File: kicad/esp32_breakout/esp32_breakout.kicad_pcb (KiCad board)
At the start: 2 copper layers, 70 x 35 mm, 26 parts, among them J1 JST B5B-PH-K-S, J10 JST B6B-PH-K-S, J2 JST B5B-PH-K-S, J3 JST B7B-PH-K-S, J4 XT30U-M, J5 HDR F 2.54MM VERT, J6 HDR F 2.54MM 5-pin VERT, J9 JST B6B-PH-K-S, SW1 SS12D10, U1 ESP32 DEV KIT Module 30-pin, U2 LM2596 Module

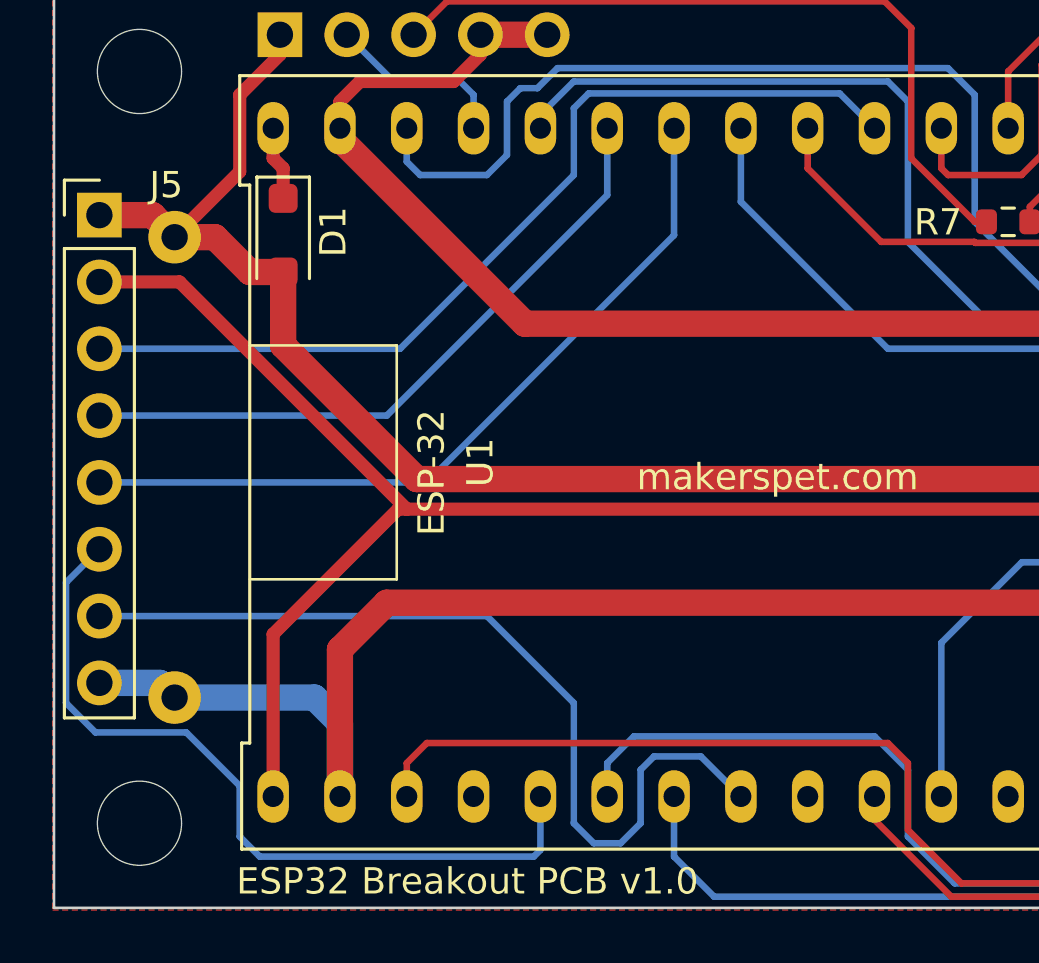
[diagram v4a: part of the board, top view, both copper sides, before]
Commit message: Footprint fix
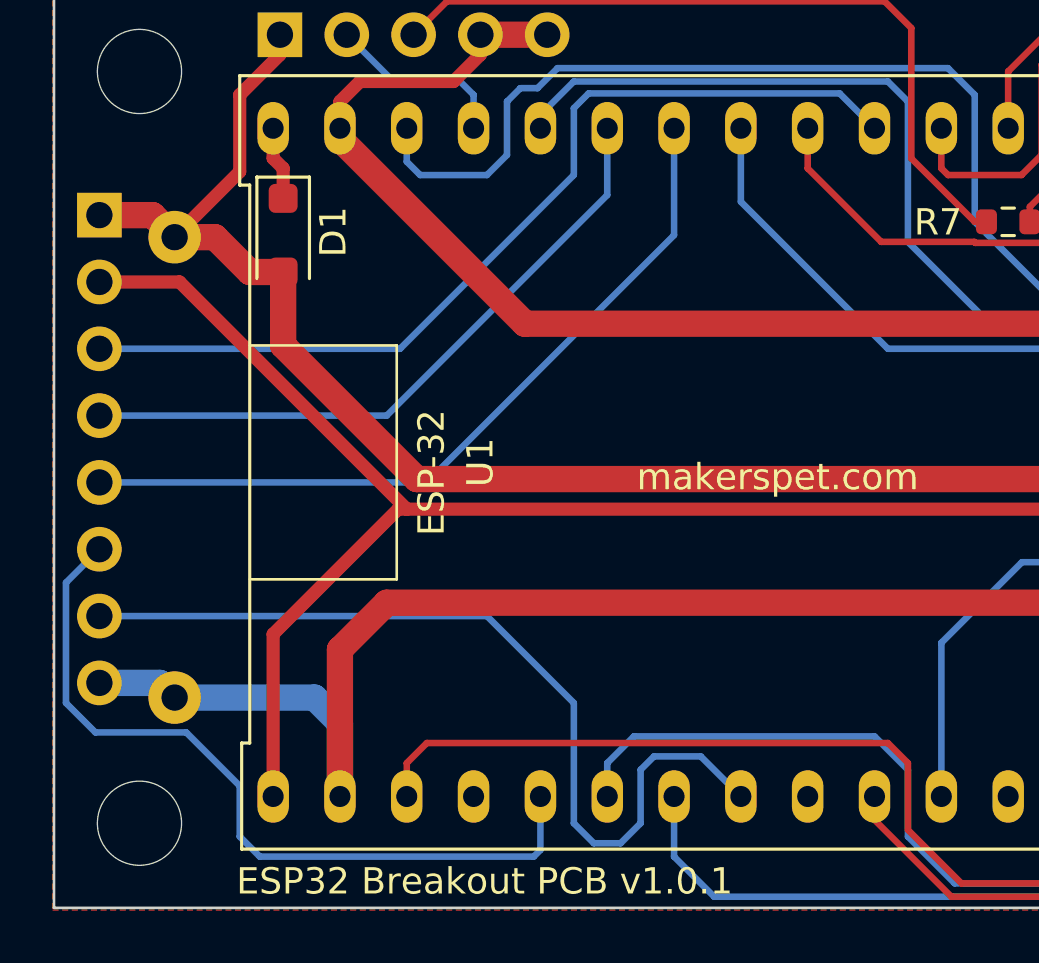
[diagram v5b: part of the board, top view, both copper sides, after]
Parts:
- J5: footprint Connector_PinHeader_2.54mm:PinHeader_1x08_P2.54mm_Vertical -> Connector_PinSocket_2.54mm:PinSocket_1x08_P2.54mm_Vertical; moved to B.Cu
- turned J5 to 180 degrees
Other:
- board text added: "ESP32 Breakout PCB v1.0.1"
- board text removed: "ESP32 Breakout PCB v1.0"
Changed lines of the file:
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@@
         (effects (font (size 1 1) (thickness 0.15)))
     )
-    (fp_text value "FS26" (at 0 1.973 90) (layer "F.Fab")
+    (fp_text value "FS26" (at 0 1.973 90) (layer "F.Fab") hide
         (effects (font (size 1 1) (thickness 0.15)))
     )
@@
     (pad "" np_thru_hole circle (at 0 0) (size 3.2 3.2) (drill 3.2) (layers "*.Cu" "*.Mask"))
   )
-  (footprint "Connector_PinHeader_2.54mm:PinHeader_1x08_P2.54mm_Vertical" (layer "F.Cu")
-    (at 127.254 86.868)
-    (descr "Through hole straight pin header, 1x08, 2.54mm pitch, single row")
-    (tags "Through hole pin header THT 1x08 2.54mm single row")
-    (property "Sheetfile" "esp32_breakout.kicad_sch")
-    (property "Sheetname" "")
-    (property "ki_description" "Generic connector, single row, 01x08, script generated (kicad-library-utils/schlib/autogen/connector/)")
-    (property "ki_keywords" "connector")
-    (attr through_hole)
-    (fp_text reference "J5" (at 2.54 -1.143) (layer "F.SilkS")
-        (effects (font (size 1 1) (thickness 0.15)))
-    )
-    (fp_text value "HDR F 2.54MM VERT" (at 2.159 9.652 90) (layer "F.Fab") hide
-        (effects (font (size 1 1) (thickness 0.15)))
-    )
-    (fp_text user "${REFERENCE}" (at -0.1016 8.9916) (layer "F.Fab")
-        (effects (font (size 1 1) (thickness 0.15)))
-    )
-    (fp_line (start -1.33 -1.33) (end 0 -1.33)
-      (stroke (width 0.12) (type solid)) (layer "F.SilkS"))
-    (fp_line (start -1.33 0) (end -1.33 -1.33)
-      (stroke (width 0.12) (type solid)) (layer "F.SilkS"))
-    (fp_line (start -1.33 1.27) (end -1.33 19.11)
-      (stroke (width 0.12) (type solid)) (layer "F.SilkS"))
-    (fp_line (start -1.33 1.27) (end 1.33 1.27)
-      (stroke (width 0.12) (type solid)) (layer "F.SilkS"))
-    (fp_line (start -1.33 19.11) (end 1.33 19.11)
-      (stroke (width 0.12) (type solid)) (layer "F.SilkS"))
-    (fp_line (start 1.33 1.27) (end 1.33 19.11)
-      (stroke (width 0.12) (type solid)) (layer "F.SilkS"))
-    (fp_line (start -1.8 -1.8) (end -1.8 19.55)
-      (stroke (width 0.05) (type solid)) (layer "F.CrtYd"))
-    (fp_line (start -1.8 19.55) (end 1.8 19.55)
-      (stroke (width 0.05) (type solid)) (layer "F.CrtYd"))
-    (fp_line (start 1.8 -1.8) (end -1.8 -1.8)
-      (stroke (width 0.05) (type solid)) (layer "F.CrtYd"))
-    (fp_line (start 1.8 19.55) (end 1.8 -1.8)
-      (stroke (width 0.05) (type solid)) (layer "F.CrtYd"))
-    (fp_line (start -1.27 -0.635) (end -0.635 -1.27)
-      (stroke (width 0.1) (type solid)) (layer "F.Fab"))
-    (fp_line (start -1.27 19.05) (end -1.27 -0.635)
-      (stroke (width 0.1) (type solid)) (layer "F.Fab"))
-    (fp_line (start -0.635 -1.27) (end 1.27 -1.27)
-      (stroke (width 0.1) (type solid)) (layer "F.Fab"))
-    (fp_line (start 1.27 -1.27) (end 1.27 19.05)
-      (stroke (width 0.1) (type solid)) (layer "F.Fab"))
-    (fp_line (start 1.27 19.05) (end -1.27 19.05)
-      (stroke (width 0.1) (type solid)) (layer "F.Fab"))
-    (pad "1" thru_hole rect (at 0 0) (size 1.7 1.7) (drill 1) (layers "*.Cu" "*.Mask")
-      (net 1 "+5V") (pinfunction "Pin_1") (pintype "passive"))
-    (pad "2" thru_hole oval (at 0 2.54) (size 1.7 1.7) (drill 1) (layers "*.Cu" "*.Mask")
-      (net 14 "+3V3") (pinfunction "Pin_2") (pintype "passive"))
-    (pad "3" thru_hole oval (at 0 5.08) (size 1.7 1.7) (drill 1) (layers "*.Cu" "*.Mask")
-      (net 15 "/GPIO32_TOUCH") (pinfunction "Pin_3") (pintype "passive"))
-    (pad "4" thru_hole oval (at 0 7.62) (size 1.7 1.7) (drill 1) (layers "*.Cu" "*.Mask")
-      (net 16 "/GPIO27_TOUCH") (pinfunction "Pin_4") (pintype "passive"))
-    (pad "5" thru_hole oval (at 0 10.16) (size 1.7 1.7) (drill 1) (layers "*.Cu" "*.Mask")
-      (net 17 "/GPIO26_TOUCH") (pinfunction "Pin_5") (pintype "passive"))
-    (pad "6" thru_hole oval (at 0 12.7) (size 1.7 1.7) (drill 1) (layers "*.Cu" "*.Mask")
-      (net 18 "/GPIO4_TOUCH") (pinfunction "Pin_6") (pintype "passive"))
-    (pad "7" thru_hole oval (at 0 15.24) (size 1.7 1.7) (drill 1) (layers "*.Cu" "*.Mask")
-      (net 21 "/GPIO5_BOOT_STRAP") (pinfunction "Pin_7") (pintype "passive"))
-    (pad "8" thru_hole oval (at 0 17.78) (size 1.7 1.7) (drill 1) (layers "*.Cu" "*.Mask")
-      (net 3 "GND") (pinfunction "Pin_8") (pintype "passive"))
-    (model "${KICAD6_3DMODEL_DIR}/Connector_PinHeader_2.54mm.3dshapes/PinHeader_1x08_P2.54mm_Vertical.wrl"
-      (offset (xyz 0 0 0))
-      (scale (xyz 1 1 1))
-      (rotate (xyz 0 0 0))
-    )
-  )
   (footprint "Resistor_SMD:R_0603_1608Metric" (layer "F.Cu")
     (at 166.878 87.122)
@@
     )
   )
+  (footprint "Connector_PinSocket_2.54mm:PinSocket_1x08_P2.54mm_Vertical" (layer "B.Cu")
+    (at 127.254 86.868 180)
+    (descr "Through hole straight socket strip, 1x08, 2.54mm pitch, single row (from Kicad 4.0.7), script generated")
+    (tags "Through hole socket strip THT 1x08 2.54mm single row")
+    (property "Sheetfile" "esp32_breakout.kicad_sch")
+    (property "Sheetname" "")
+    (property "ki_description" "Generic connector, single row, 01x08, script generated (kicad-library-utils/schlib/autogen/connector/)")
+    (property "ki_keywords" "connector")
+    (attr through_hole)
+    (fp_text reference "J5" (at 0 2.77) (layer "B.SilkS")
+        (effects (font (size 1 1) (thickness 0.15)) (justify mirror))
+    )
+    (fp_text value "HDR F 2.54MM VERT" (at 0 -20.55) (layer "B.Fab") hide
+        (effects (font (size 1 1) (thickness 0.15)) (justify mirror))
+    )
+    (fp_text user "${REFERENCE}" (at 0 -8.89 90) (layer "B.Fab")
+        (effects (font (size 1 1) (thickness 0.15)) (justify mirror))
+    )
+    (fp_line (start -1.33 -19.11) (end 1.33 -19.11)
+      (stroke (width 0.12) (type solid)) (layer "B.SilkS"))
+    (fp_line (start -1.33 -1.27) (end -1.33 -19.11)
+      (stroke (width 0.12) (type solid)) (layer "B.SilkS"))
+    (fp_line (start -1.33 -1.27) (end 1.33 -1.27)
+      (stroke (width 0.12) (type solid)) (layer "B.SilkS"))
+    (fp_line (start 0 1.33) (end 1.33 1.33)
+      (stroke (width 0.12) (type solid)) (layer "B.SilkS"))
+    (fp_line (start 1.33 -1.27) (end 1.33 -19.11)
+      (stroke (width 0.12) (type solid)) (layer "B.SilkS"))
+    (fp_line (start 1.33 1.33) (end 1.33 0)
+      (stroke (width 0.12) (type solid)) (layer "B.SilkS"))
+    (fp_line (start -1.8 -19.55) (end -1.8 1.8)
+      (stroke (width 0.05) (type solid)) (layer "B.CrtYd"))
+    (fp_line (start -1.8 1.8) (end 1.75 1.8)
+      (stroke (width 0.05) (type solid)) (layer "B.CrtYd"))
+    (fp_line (start 1.75 -19.55) (end -1.8 -19.55)
+      (stroke (width 0.05) (type solid)) (layer "B.CrtYd"))
+    (fp_line (start 1.75 1.8) (end 1.75 -19.55)
+      (stroke (width 0.05) (type solid)) (layer "B.CrtYd"))
+    (fp_line (start -1.27 -19.05) (end -1.27 1.27)
+      (stroke (width 0.1) (type solid)) (layer "B.Fab"))
+    (fp_line (start -1.27 1.27) (end 0.635 1.27)
+      (stroke (width 0.1) (type solid)) (layer "B.Fab"))
+    (fp_line (start 0.635 1.27) (end 1.27 0.635)
+      (stroke (width 0.1) (type solid)) (layer "B.Fab"))
+    (fp_line (start 1.27 -19.05) (end -1.27 -19.05)
+      (stroke (width 0.1) (type solid)) (layer "B.Fab"))
+    (fp_line (start 1.27 0.635) (end 1.27 -19.05)
+      (stroke (width 0.1) (type solid)) (layer "B.Fab"))
+    (pad "1" thru_hole rect (at 0 0 180) (size 1.7 1.7) (drill 1) (layers "*.Cu" "*.Mask")
+      (net 1 "+5V") (pinfunction "Pin_1") (pintype "passive"))
+    (pad "2" thru_hole oval (at 0 -2.54 180) (size 1.7 1.7) (drill 1) (layers "*.Cu" "*.Mask")
+      (net 14 "+3V3") (pinfunction "Pin_2") (pintype "passive"))
+    (pad "3" thru_hole oval (at 0 -5.08 180) (size 1.7 1.7) (drill 1) (layers "*.Cu" "*.Mask")
+      (net 15 "/GPIO32_TOUCH") (pinfunction "Pin_3") (pintype "passive"))
+    (pad "4" thru_hole oval (at 0 -7.62 180) (size 1.7 1.7) (drill 1) (layers "*.Cu" "*.Mask")
+      (net 16 "/GPIO27_TOUCH") (pinfunction "Pin_4") (pintype "passive"))
+    (pad "5" thru_hole oval (at 0 -10.16 180) (size 1.7 1.7) (drill 1) (layers "*.Cu" "*.Mask")
+      (net 17 "/GPIO26_TOUCH") (pinfunction "Pin_5") (pintype "passive"))
+    (pad "6" thru_hole oval (at 0 -12.7 180) (size 1.7 1.7) (drill 1) (layers "*.Cu" "*.Mask")
+      (net 18 "/GPIO4_TOUCH") (pinfunction "Pin_6") (pintype "passive"))
+    (pad "7" thru_hole oval (at 0 -15.24 180) (size 1.7 1.7) (drill 1) (layers "*.Cu" "*.Mask")
+      (net 21 "/GPIO5_BOOT_STRAP") (pinfunction "Pin_7") (pintype "passive"))
+    (pad "8" thru_hole oval (at 0 -17.78 180) (size 1.7 1.7) (drill 1) (layers "*.Cu" "*.Mask")
+      (net 3 "GND") (pinfunction "Pin_8") (pintype "passive"))
+    (model "${KICAD6_3DMODEL_DIR}/Connector_PinSocket_2.54mm.3dshapes/PinSocket_1x08_P2.54mm_Vertical.wrl"
+      (offset (xyz 0 0 0))
+      (scale (xyz 1 1 1))
+      (rotate (xyz 0 0 0))
+    )
+  )
   (footprint "Connector_PinSocket_2.54mm:PinSocket_1x05_P2.54mm_Vertical" (layer "B.Cu")
     (at 134.117 80.01 -90)
@@
     (effects (font (size 1 1) (thickness 0.15)) (justify bottom))
   )
-  (gr_text "ESP32 Breakout PCB v1.0" (at 132.461 112.776) (layer "F.SilkS")
+  (gr_text "ESP32 Breakout PCB v1.0.1" (at 132.461 112.776) (layer "F.SilkS")
     (effects (font (size 1 1) (thickness 0.15)) (justify left bottom))
   )

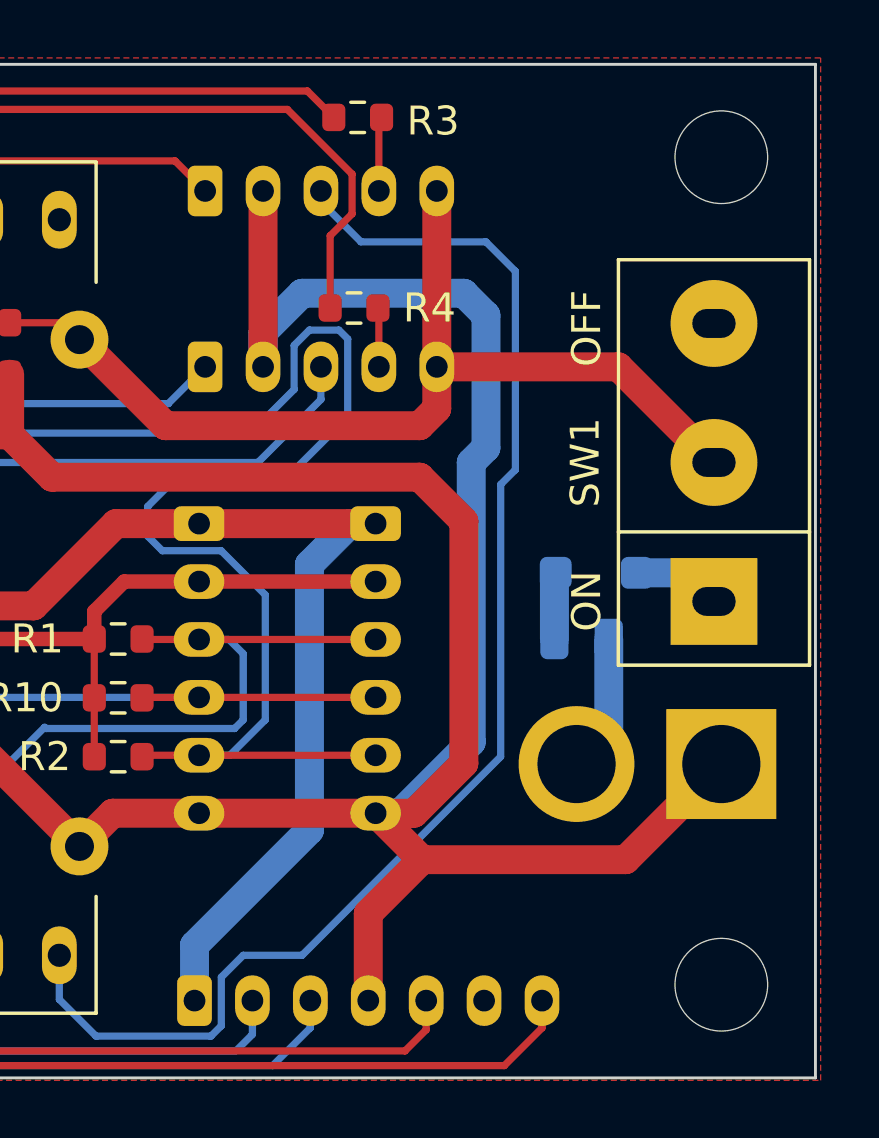
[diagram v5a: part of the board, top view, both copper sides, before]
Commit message: Alt fuse; fan fix
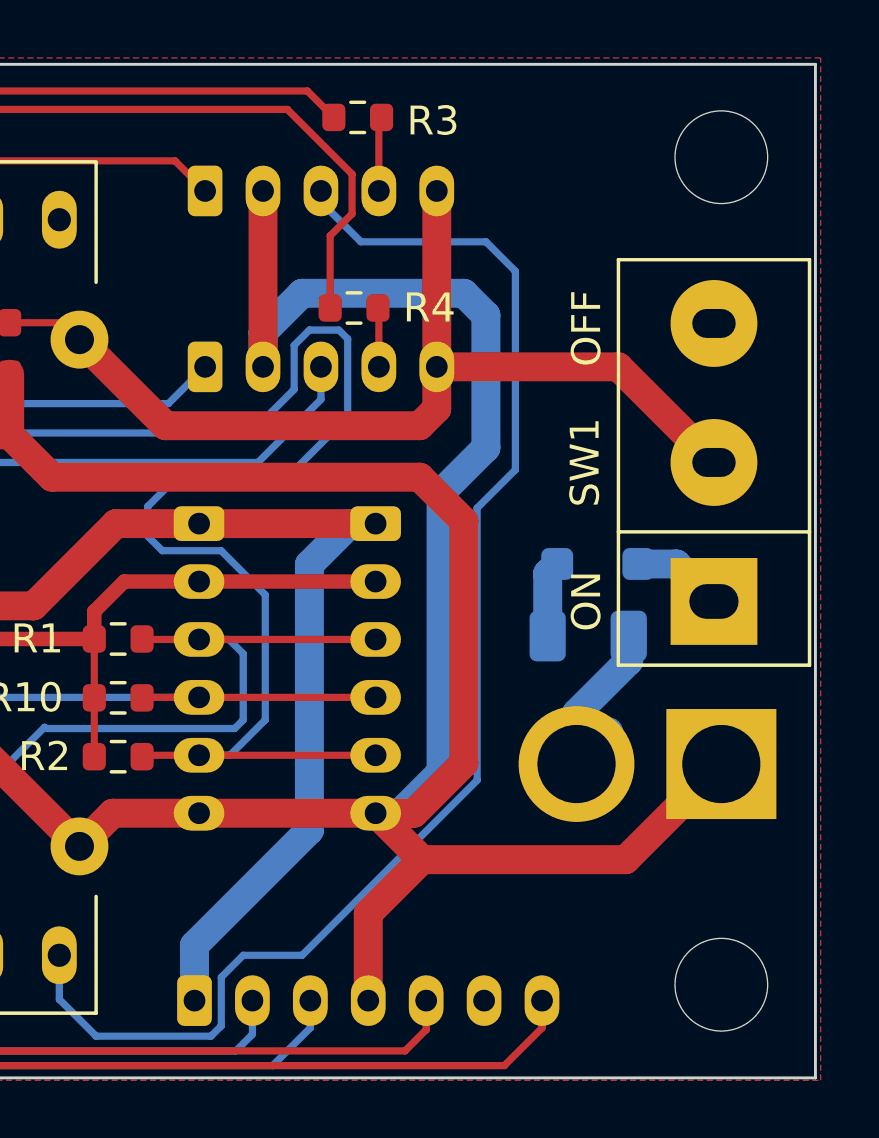
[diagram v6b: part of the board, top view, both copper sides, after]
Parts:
- F1: value FCC20202AATP -> 0685T2500-01; footprint Fuse:Fuse_0805_2012Metric -> Fuse:Fuse_1206_3216Metric
- moved D2 0.31 mm to (188.0, 95.5)
- moved F1 0.25 mm to (187.7, 97.9)
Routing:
- net Net-(J4-+): track 4.78 -> 6.74 mm

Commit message: ESP32 PCB v1.1.0
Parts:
- J5: value HDR F 2.54MM VERT -> HDR 8p M VERT 2.54mm; footprint Connector_PinSocket_2.54mm:PinSocket_1x08_P2.54mm_Vertical -> Connector_PinHeader_2.54mm:PinHeader_1x08_P2.54mm_Vertical
- J6: value HDR F 2.54MM 5-pin VERT -> JST B5B-ZR; footprint Connector_PinSocket_2.54mm:PinSocket_1x05_P2.54mm_Vertical -> Makerspet:JST_ZH_B5B-ZR_1x05_P1.50mm_Vertical
- moved J6 10.9 mm to (123.6, 82.6)
- moved J5 6.71 mm to (123.5, 92.5)
- moved J4 6.13 mm to (186.2, 103.4), turned to 90 degrees
- moved R3 5.79 mm to (179.7, 85.8)
- moved F1 5.17 mm to (186.6, 92.9), turned to 90 degrees
- moved R1 3.07 mm to (168.4, 98.0)
- moved R10 3.07 mm to (168.4, 100.1)
- moved R2 3.07 mm to (168.4, 102.1)
- moved D2 2.74 mm to (189.0, 92.9), turned to 90 degrees
- moved H1 1.71 mm to (129.5, 83.0)
- moved SW1 1.63 mm to (192.0, 93.6)
- moved H2 1.56 mm to (192.2, 83.0)
- moved J2 1.30 mm to (174.5, 83.9)
- moved U2 1.01 mm to (149.1, 96.3)
- moved J3 0.79 mm to (174.5, 109.9)
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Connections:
- net /LDS_MOT_EN renamed /LDS_EN
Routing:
- net GND: track 195.7 -> 221.6 mm
- net /GPIO12_OUT_STRAP: track 7.04 -> 26.0 mm
- net Net-(J6-Pin_3): track 28.7 -> 43.6 mm
- net /GPIO32_TOUCH: track 35.5 -> 41.5 mm
- net /GPIO27_TOUCH: track 25.3 -> 31.3 mm
- net /GPIO26_TOUCH: track 29.8 -> 35.8 mm
- net /GPIO4_TOUCH: track 30.1 -> 25.1 mm
- net /GPIO5_BOOT_STRAP: track 33.8 -> 37.6 mm
- net +3V3: track 75.3 -> 78.7 mm
- net /MOT_FG_LEFT: track 20.6 -> 23.9 mm
- net /MOT_FG_RIGHT: track 32.1 -> 29.3 mm
- net Net-(J4-+): track 6.74 -> 4.24 mm
- net /I2C_SDA: track 30.2 -> 32.7 mm
- net /I2C_SCL: track 27.8 -> 30.3 mm
- net +5V: track 89.3 -> 91.7 mm
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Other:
- board size 70 x 35 mm -> 73.8 x 33.1 mm
- board text added: "+ BATT -"
- board text added: "ESP32 Breakout PCB v1.1.0"
- board text added: "LASER DIST"
- board text added: "LEFT RIGHT"
- board text added: "U.DIST"
- board text removed: "BATT"
- board text removed: "DIST"
- board text removed: "ESP32 Breakout PCB v1.0.1"
- board text removed: "LEFT"
- board text removed: "RIGHT"
